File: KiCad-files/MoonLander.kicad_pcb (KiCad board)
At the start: 2 copper layers, 37.8 x 22.7 mm, 88 parts, among them IC1 MCP73831/2, IC2 BU33SD5, IC3 PRTR5V0U2X, IC4 CP2110-GM, IC5 LPC824M201JHI33, J1 Cortex_JTAG/SWD_10, P1 CONN_01X02, P2 CONN_01X02, P3 USB_OTG, P4 CONN_02X08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

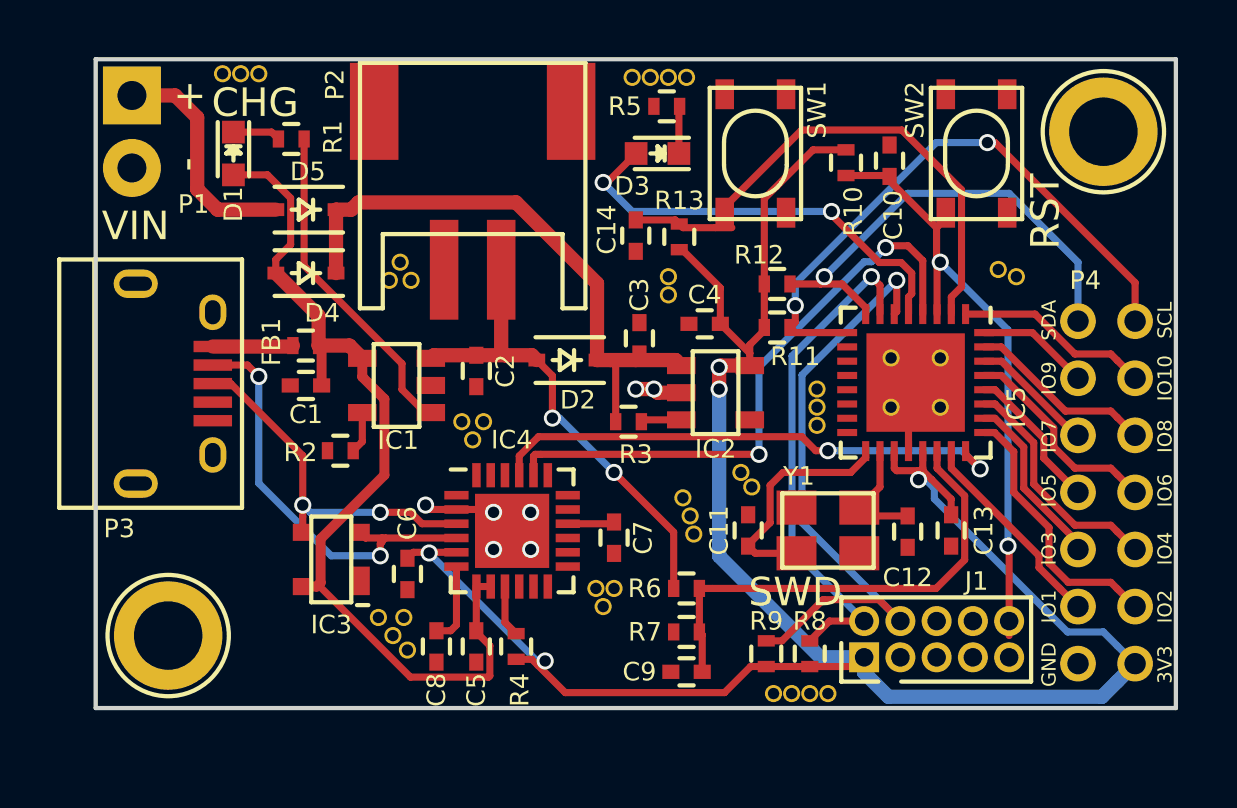
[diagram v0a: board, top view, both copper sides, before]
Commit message: added I2C EEPROM, redid ground stitching
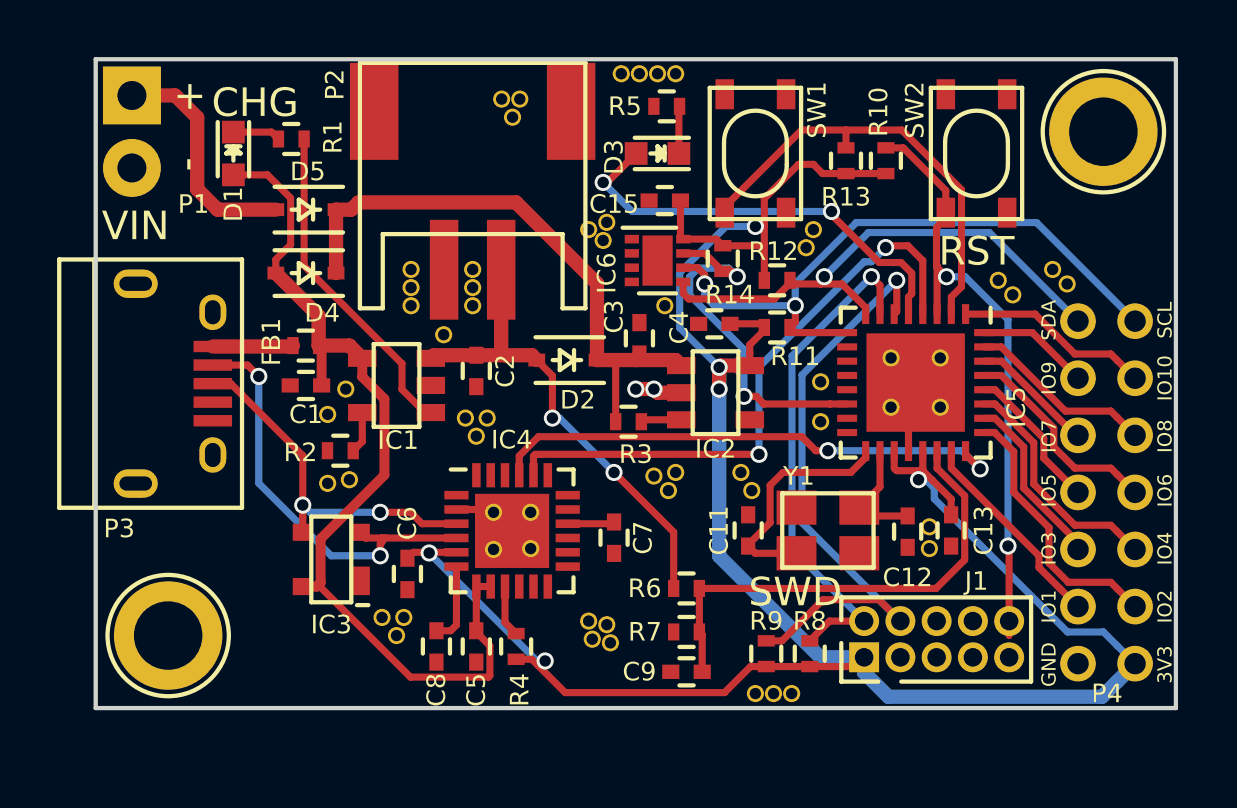
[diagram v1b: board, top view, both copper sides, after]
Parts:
- removed C10, C14: 0.1uF, Capacitors_SMD:C_0402
- removed the REF** at (139.6, 94.5)
- removed the REF** at (139.2, 106.3)
- removed the REF** at (147.1, 105.9)
- removed the REF** at (147.4, 105.3)
- removed the REF** at (146.8, 105.3)
- removed the REF** at (154.3, 109.0)
- removed the REF** at (154.9, 109.0)
- removed the REF** at (152.3, 101.7)
- removed the REF** at (140.3, 94.5)
- removed the REF** at (150.2, 103.4)
- removed the REF** at (150.1, 102.7)
- removed the REF** at (149.9, 102.1)
- removed the REF** at (154.6, 99.6)
- removed the REF** at (154.6, 98.9)
- removed the REF** at (154.6, 98.3)
- removed the REF** at (140.0, 93.9)
- removed the REF** at (161.5, 94.4)
- removed the REF** at (160.9, 94.1)
- removed the REF** at (149.4, 95.0)
- removed the REF** at (149.4, 94.4)
- removed the REF** at (150.0, 87.4)
- removed the REF** at (149.4, 87.4)
- removed the REF** at (148.7, 87.4)
- removed the REF** at (148.1, 87.4)
- removed the REF** at (135.0, 87.2)
- removed the REF** at (134.4, 87.2)
- removed the REF** at (142.5, 100.1)
- removed the REF** at (133.7, 87.2)
- removed the REF** at (142.9, 99.4)
- removed the REF** at (142.1, 99.4)
- removed the REF** at (140.2, 107.4)
- removed the REF** at (139.7, 106.9)
- added C15: 0.1uF, Capacitors_SMD:C_0402, F.Cu at (149.2, 91.7)
- added IC6: 24LCxx, Housings_DFN_QFN:DFN-8-1EP_2x2mm_Pitch0.5mm, F.Cu at (149.0, 93.8)
- added R14: 10k, Resistors_SMD:R_0402, F.Cu at (151.3, 93.7)
- added REF**: STITCH_VIA, GrayCatLabs:STITCH_VIA, F.Cu at (149.2, 95.4)
- added REF**: STITCH_VIA, GrayCatLabs:STITCH_VIA, F.Cu at (137.4, 101.6)
- added REF**: STITCH_VIA, GrayCatLabs:STITCH_VIA, F.Cu at (138.0, 98.3)
- added REF**: STITCH_VIA, GrayCatLabs:STITCH_VIA, F.Cu at (137.4, 99.2)
- added REF**: STITCH_VIA, GrayCatLabs:STITCH_VIA, F.Cu at (142.6, 99.9)
- added REF**: STITCH_VIA, GrayCatLabs:STITCH_VIA, F.Cu at (143.0, 99.3)
- added REF**: STITCH_VIA, GrayCatLabs:STITCH_VIA, F.Cu at (142.2, 99.3)
- added REF**: STITCH_VIA, GrayCatLabs:STITCH_VIA, F.Cu at (143.9, 88.8)
- added REF**: STITCH_VIA, GrayCatLabs:STITCH_VIA, F.Cu at (143.5, 88.1)
- added REF**: STITCH_VIA, GrayCatLabs:STITCH_VIA, F.Cu at (144.1, 88.1)
- added REF**: STITCH_VIA, GrayCatLabs:STITCH_VIA, F.Cu at (162.8, 94.1)
- added REF**: STITCH_VIA, GrayCatLabs:STITCH_VIA, F.Cu at (146.6, 92.7)
- added REF**: STITCH_VIA, GrayCatLabs:STITCH_VIA, F.Cu at (163.3, 94.6)
- added REF**: STITCH_VIA, GrayCatLabs:STITCH_VIA, F.Cu at (161.4, 95.0)
- added REF**: STITCH_VIA, GrayCatLabs:STITCH_VIA, F.Cu at (160.9, 94.5)
- added REF**: STITCH_VIA, GrayCatLabs:STITCH_VIA, F.Cu at (154.2, 93.3)
- added REF**: STITCH_VIA, GrayCatLabs:STITCH_VIA, F.Cu at (154.4, 92.7)
- added REF**: STITCH_VIA, GrayCatLabs:STITCH_VIA, F.Cu at (142.5, 95.4)
- added REF**: STITCH_VIA, GrayCatLabs:STITCH_VIA, F.Cu at (142.5, 94.7)
- added REF**: STITCH_VIA, GrayCatLabs:STITCH_VIA, F.Cu at (142.5, 94.1)
- added REF**: STITCH_VIA, GrayCatLabs:STITCH_VIA, F.Cu at (141.5, 96.4)
- added REF**: STITCH_VIA, GrayCatLabs:STITCH_VIA, F.Cu at (140.3, 95.4)
- added REF**: STITCH_VIA, GrayCatLabs:STITCH_VIA, F.Cu at (147.1, 93.1)
- added REF**: STITCH_VIA, GrayCatLabs:STITCH_VIA, F.Cu at (140.3, 94.7)
- added REF**: STITCH_VIA, GrayCatLabs:STITCH_VIA, F.Cu at (140.3, 94.1)
- added REF**: STITCH_VIA, GrayCatLabs:STITCH_VIA, F.Cu at (146.6, 106.4)
- added REF**: STITCH_VIA, GrayCatLabs:STITCH_VIA, F.Cu at (146.7, 107.1)
- added REF**: STITCH_VIA, GrayCatLabs:STITCH_VIA, F.Cu at (147.3, 107.2)
- added REF**: STITCH_VIA, GrayCatLabs:STITCH_VIA, F.Cu at (147.2, 106.6)
- added REF**: STITCH_VIA, GrayCatLabs:STITCH_VIA, F.Cu at (152.4, 109.0)
- added REF**: STITCH_VIA, GrayCatLabs:STITCH_VIA, F.Cu at (149.6, 87.2)
- added REF**: STITCH_VIA, GrayCatLabs:STITCH_VIA, F.Cu at (147.2, 92.5)
- added REF**: STITCH_VIA, GrayCatLabs:STITCH_VIA, F.Cu at (149.0, 87.2)
- added REF**: STITCH_VIA, GrayCatLabs:STITCH_VIA, F.Cu at (148.3, 87.2)
- added REF**: STITCH_VIA, GrayCatLabs:STITCH_VIA, F.Cu at (147.7, 87.2)
- added REF**: STITCH_VIA, GrayCatLabs:STITCH_VIA, F.Cu at (139.8, 106.9)
- added REF**: STITCH_VIA, GrayCatLabs:STITCH_VIA, F.Cu at (139.3, 106.3)
- added REF**: STITCH_VIA, GrayCatLabs:STITCH_VIA, F.Cu at (143.2, 103.9)
- added REF**: STITCH_VIA, GrayCatLabs:STITCH_VIA, F.Cu at (144.5, 103.9)
- added REF**: STITCH_VIA, GrayCatLabs:STITCH_VIA, F.Cu at (144.5, 102.6)
- added REF**: STITCH_VIA, GrayCatLabs:STITCH_VIA, F.Cu at (143.2, 102.6)
- added REF**: STITCH_VIA, GrayCatLabs:STITCH_VIA, F.Cu at (158.5, 103.9)
- added REF**: STITCH_VIA, GrayCatLabs:STITCH_VIA, F.Cu at (149.6, 101.2)
- added REF**: STITCH_VIA, GrayCatLabs:STITCH_VIA, F.Cu at (149.4, 101.9)
- added REF**: STITCH_VIA, GrayCatLabs:STITCH_VIA, F.Cu at (148.8, 101.3)
- added REF**: STITCH_VIA, GrayCatLabs:STITCH_VIA, F.Cu at (154.7, 98.0)
- added REF**: STITCH_VIA, GrayCatLabs:STITCH_VIA, F.Cu at (154.7, 99.4)
- added REF**: STITCH_VIA, GrayCatLabs:STITCH_VIA, F.Cu at (158.5, 103.1)
- added REF**: STITCH_VIA, GrayCatLabs:STITCH_VIA, F.Cu at (152.3, 101.9)
- added REF**: STITCH_VIA, GrayCatLabs:STITCH_VIA, F.Cu at (138.2, 101.5)
- moved R13 6.42 mm to (155.6, 90.3), turned to 270 degrees
- moved R10 1.40 mm to (157.0, 90.3), turned to 90 degrees
- moved C4 0.34 mm to (151.0, 96.0)
- moved R12 0.13 mm to (153.2, 94.5)
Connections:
- IC5 pad 14: Net-(IC5-Pad14) -> /CPU/EEPROM_WP
- R13 pad 1: VCC -> /CPU/ISP_ENTRY
- R13 pad 2: /CPU/ISP_ENTRY -> VCC
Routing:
- net /CPU/EEPROM_WP: track 0.00 -> 12.9 mm, vias 0 -> 2
- net VCC: track 75.7 -> 84.5 mm, vias 5 -> 6
- net /CPU/ISP_ENTRY: track 18.5 -> 15.6 mm
- net /CPU/I2C0_SDA: track 16.7 -> 19.0 mm
- net /CPU/I2C0_SCL: track 21.0 -> 22.8 mm
- net GND: track 5.14 -> 4.00 mm, vias 7 -> 2

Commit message: fixed header symbol/footprint naming, minor changes
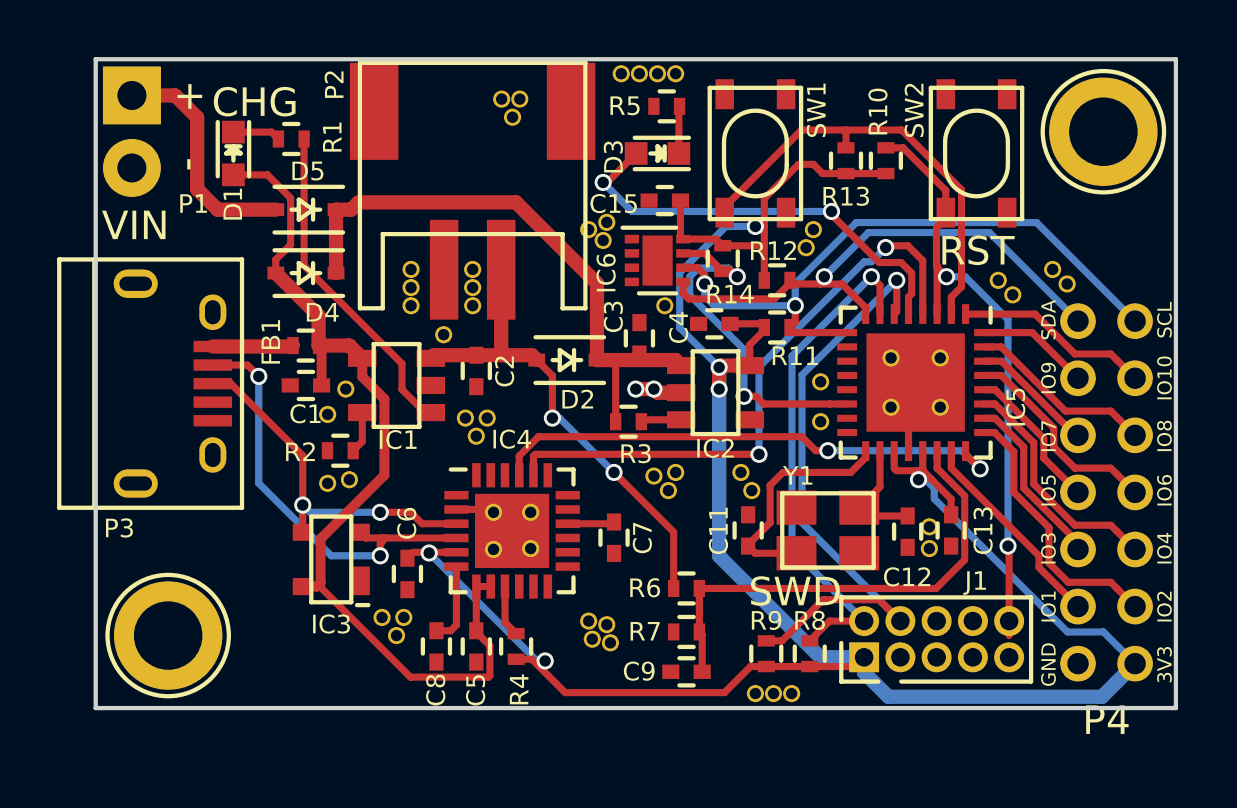
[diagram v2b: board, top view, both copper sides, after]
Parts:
- P4: value CONN_02X08 -> CONN_02X07; footprint GrayCatLabs:Header_2mm_2x6 -> GrayCatLabs:Header_2mm_2x7

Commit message: drive ISP_ENTRY and RST from CP2110 GPIO outputs
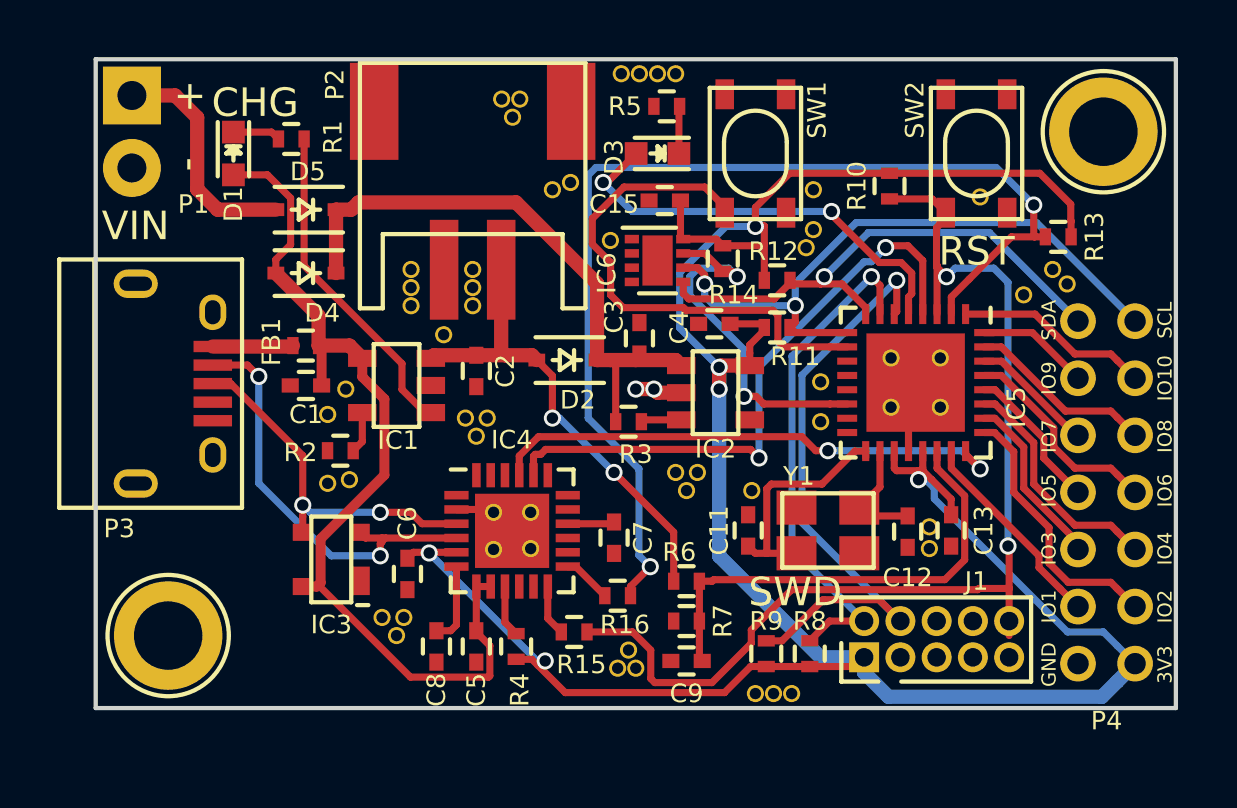
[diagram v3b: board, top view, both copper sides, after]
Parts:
- removed the REF** at (149.2, 95.4)
- removed the REF** at (160.9, 94.5)
- removed the REF** at (147.2, 106.6)
- removed the REF** at (151.9, 101.2)
- added R15: 100, Resistors_SMD:R_0402, F.Cu at (146.1, 106.8)
- added R16: 100, Resistors_SMD:R_0402, F.Cu at (147.6, 105.5)
- added REF**: STITCH_VIA, GrayCatLabs:STITCH_VIA, F.Cu at (154.4, 91.3)
- added REF**: STITCH_VIA, GrayCatLabs:STITCH_VIA, F.Cu at (160.3, 91.6)
- moved R13 7.90 mm to (163.0, 93.0), turned to 0 degrees
- moved REF** 2.33 mm to (148.2, 108.1)
- moved REF** 1.89 mm to (145.9, 91.1)
- moved REF** 1.89 mm to (145.3, 91.3)
- moved REF** 1.35 mm to (147.6, 108.1)
- moved REF** 1.25 mm to (150.0, 101.9)
- moved REF** 1.20 mm to (150.4, 101.2)
- moved R10 0.90 mm to (157.1, 91.2), turned to 270 degrees
- moved REF** 0.68 mm to (148.0, 107.4)
- moved C9 0.38 mm to (150.0, 107.8)
- moved R7 0.38 mm to (150.0, 106.4)
- moved REF** 0.38 mm to (161.8, 95.0)
- moved R6 0.25 mm to (150.0, 105.0)
- moved REF** 0.25 mm to (147.3, 93.1)
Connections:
- IC4 pad 12: Net-(IC4-Pad12) -> /CPU/ISP_RST
- IC4 pad 13: Net-(IC4-Pad13) -> /CPU/ISP_ENTRY
- IC5 pad 10: Net-(IC5-Pad10) -> /CPU/SW1
- IC5 pad 2: /CPU/ISP_ENTRY -> Net-(IC5-Pad2)
- R13 pad 1: /CPU/ISP_ENTRY -> Net-(IC5-Pad2)
- SW1 pad 1: /CPU/ISP_ENTRY -> /CPU/SW1
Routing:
- net Net-(IC5-Pad2): track 0.00 -> 38.1 mm, vias 0 -> 2
- net /CPU/SW1: track 0.00 -> 18.1 mm
- net /CPU/RESET: track 21.6 -> 39.0 mm
- net /CPU/ISP_ENTRY: track 15.6 -> 1.72 mm
- net VCC: track 84.5 -> 92.4 mm
- net /CPU/ISP_RST: track 0.00 -> 1.79 mm
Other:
- board text added: "MoonLander Rev.B"
- board text removed: "MoonLander RevB"

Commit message: moved SWD header a bit
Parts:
- moved J1 0.64 mm to (155.6, 107.7)
- moved R8 0.51 mm to (153.8, 107.6)
- moved R9 0.51 mm to (152.3, 107.6)
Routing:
- net VCC: track 92.4 -> 91.6 mm
